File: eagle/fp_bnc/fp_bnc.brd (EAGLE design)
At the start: 77.6 x 26.6 mm, 12 parts, among them J1 031-5329-52RFX, J2 031-5329-52RFX, J5 TSM-110-01-S-SV

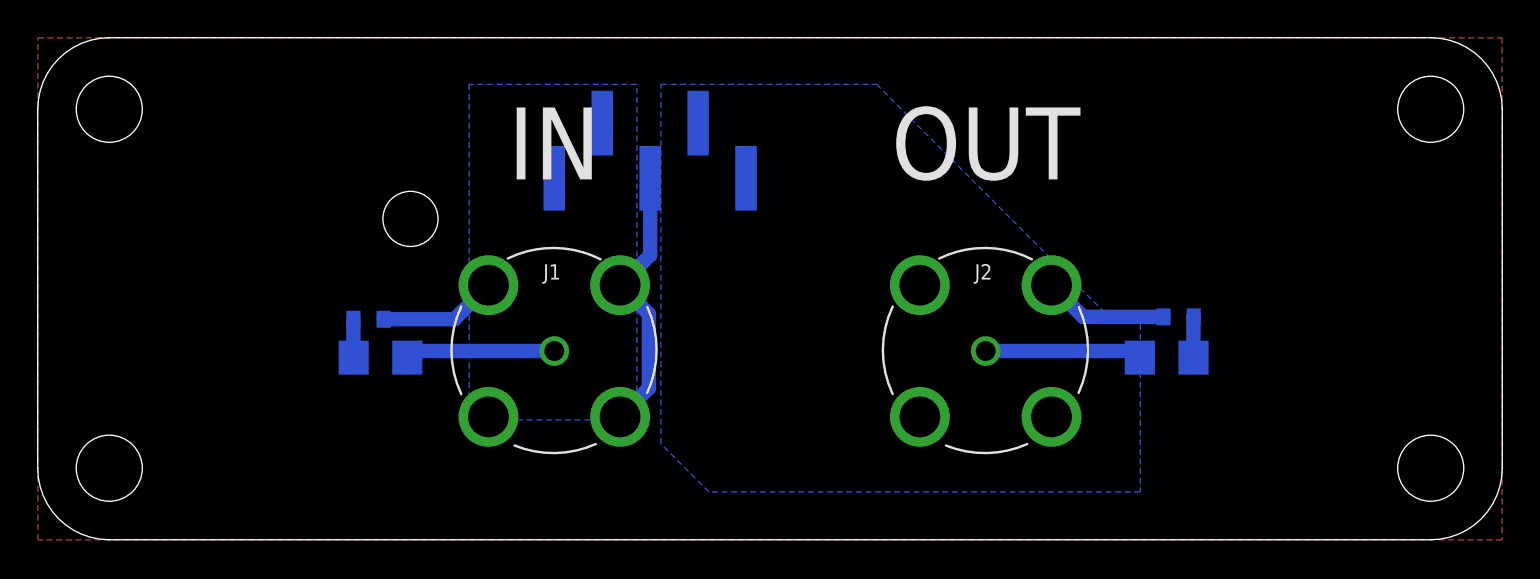
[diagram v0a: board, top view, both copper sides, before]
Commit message: Pre-production update.
* Increased clearances from chassis/enclosure ground.
* Improved text.
* Added gerbers.
* Added USB back panel.
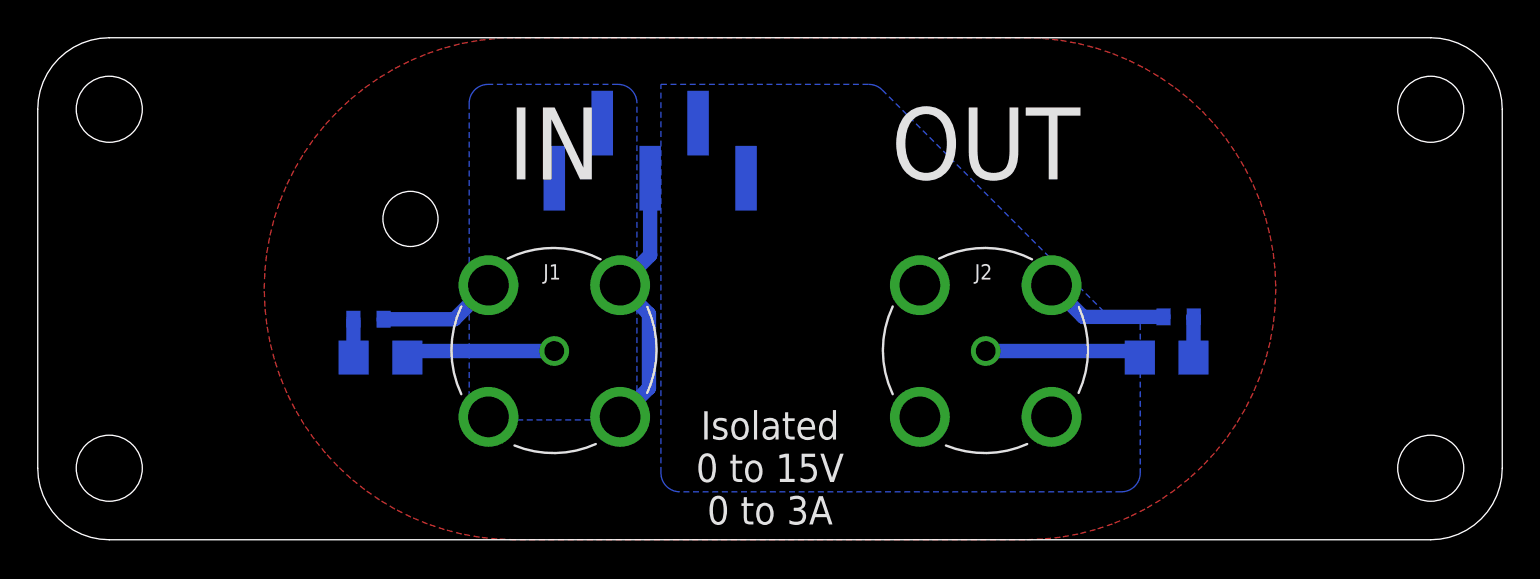
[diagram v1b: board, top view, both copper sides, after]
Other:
- board text added: "Isolated 0 to 15V 0 to 3A"
- board text added: "Joulescope Front Panel: BNC Jacks rev D 2019 Jetperch LLC"
- board text removed: "Joulescope Front Panel: BNC Jacks rev C c 2018 Jetperch LLC"
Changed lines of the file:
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@@
 <?xml version="1.0" encoding="utf-8"?>
 <!DOCTYPE eagle SYSTEM "eagle.dtd">
-<eagle version="9.2.2">
+<eagle version="9.3.2">
 <drawing>
 <settings>
@@
 <layer number="132" name="bAdjust" color="7" fill="1" visible="yes" active="yes"/>
 <layer number="144" name="Drill_legend" color="7" fill="1" visible="yes" active="yes"/>
-<layer number="145" name="DrillLegend_01-16" color="2" fill="9" visible="no" active="yes"/>
-<layer number="146" name="DrillLegend_01-20" color="3" fill="9" visible="no" active="yes"/>
+<layer number="145" name="DrillLegend_01-16" color="2" fill="9" visible="yes" active="yes"/>
+<layer number="146" name="DrillLegend_01-20" color="3" fill="9" visible="yes" active="yes"/>
 <layer number="150" name="Notes" color="7" fill="1" visible="yes" active="yes"/>
 <layer number="151" name="HeatSink" color="7" fill="1" visible="yes" active="yes"/>
@@
 <text x="27.37" y="21" size="3.81" layer="121" font="vector" ratio="20" align="center">IN</text>
 <text x="50.23" y="21" size="3.81" layer="121" font="vector" ratio="20" align="center">OUT</text>
-<text x="38.8" y="3.01" size="1.27" layer="122" font="vector" ratio="20" rot="MR0" align="center">Joulescope Front Panel: BNC Jacks rev C
- c  2018 Jetperch LLC</text>
-<circle x="46.99" y="1.867" radius="1.016" width="0.254" layer="122"/>
+<text x="38.8" y="2.5" size="1.27" layer="122" font="vector" ratio="20" rot="MR0" align="center">Joulescope Front Panel: BNC Jacks rev D
+2019 Jetperch LLC</text>
 <dimension x1="0" y1="22.81" x2="77.6" y2="19.05" x3="38.8" y3="31.75" textsize="1.778" layer="47" dtype="horizontal"/>
 <dimension x1="3.79" y1="0" x2="7.62" y2="26.6" x3="-6.35" y3="13.3" textsize="1.778" layer="47" dtype="vertical"/>
@@
 <rectangle x1="0" y1="0" x2="1.5" y2="26.6" layer="40"/>
 <rectangle x1="76.1" y1="0" x2="77.6" y2="26.6" layer="40"/>
+<text x="38.8" y="3.81" size="1.5" layer="121" font="vector" ratio="20" align="center">Isolated
+0 to 15V
+0 to 3A</text>
 </plain>
 <attributes>
@@
 <contactref element="J5" pad="1"/>
 <polygon width="0.254" layer="16" isolate="0.254" thermals="no">
-<vertex x="31.75" y="24.13"/>
-<vertex x="22.86" y="24.13"/>
+<vertex x="31.75" y="6.35"/>
+<vertex x="31.75" y="23.13" curve="90"/>
+<vertex x="30.75" y="24.13"/>
+<vertex x="23.86" y="24.13" curve="90"/>
+<vertex x="22.86" y="23.13"/>
 <vertex x="22.86" y="6.35"/>
-<vertex x="31.75" y="6.35"/>
 </polygon>
 <contactref element="R2" pad="2"/>
@@
 <signal name="EXT_NEG">
 <contactref element="J5" pad="3"/>
-<polygon width="0.1524" layer="1" thermals="no">
-<vertex x="0" y="0"/>
-<vertex x="0" y="26.6"/>
-<vertex x="77.6" y="26.6"/>
-<vertex x="77.6" y="0"/>
+<polygon width="0.254" layer="1" thermals="no">
+<vertex x="52.3" y="0"/>
+<vertex x="25.3" y="0" curve="-90"/>
+<vertex x="12" y="13.3" curve="-90"/>
+<vertex x="25.3" y="26.6"/>
+<vertex x="52.3" y="26.6" curve="-90"/>
+<vertex x="65.6" y="13.3" curve="-90"/>
 </polygon>
 <contactref element="C2" pad="1"/>
@@
 <polygon width="0.254" layer="16" isolate="0.254" thermals="no">
 <vertex x="33.02" y="24.13"/>
-<vertex x="44.45" y="24.13"/>
+<vertex x="44.0357875" y="24.13" curve="-45"/>
+<vertex x="44.74289375" y="23.83710625"/>
 <vertex x="56.642" y="11.938"/>
 <vertex x="58.42" y="11.938"/>
-<vertex x="58.42" y="2.54"/>
-<vertex x="35.56" y="2.54"/>
-<vertex x="33.02" y="5.08"/>
+<vertex x="58.42" y="3.54" curve="-90"/>
+<vertex x="57.42" y="2.54"/>
+<vertex x="34.02" y="2.54" curve="-90"/>
+<vertex x="33.02" y="3.54"/>
 </polygon>
 <contactref element="R1" pad="2"/>
